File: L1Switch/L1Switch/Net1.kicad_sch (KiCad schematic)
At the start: 31 parts, among them J2 Conn_01x07_Male, U2 VSC8658

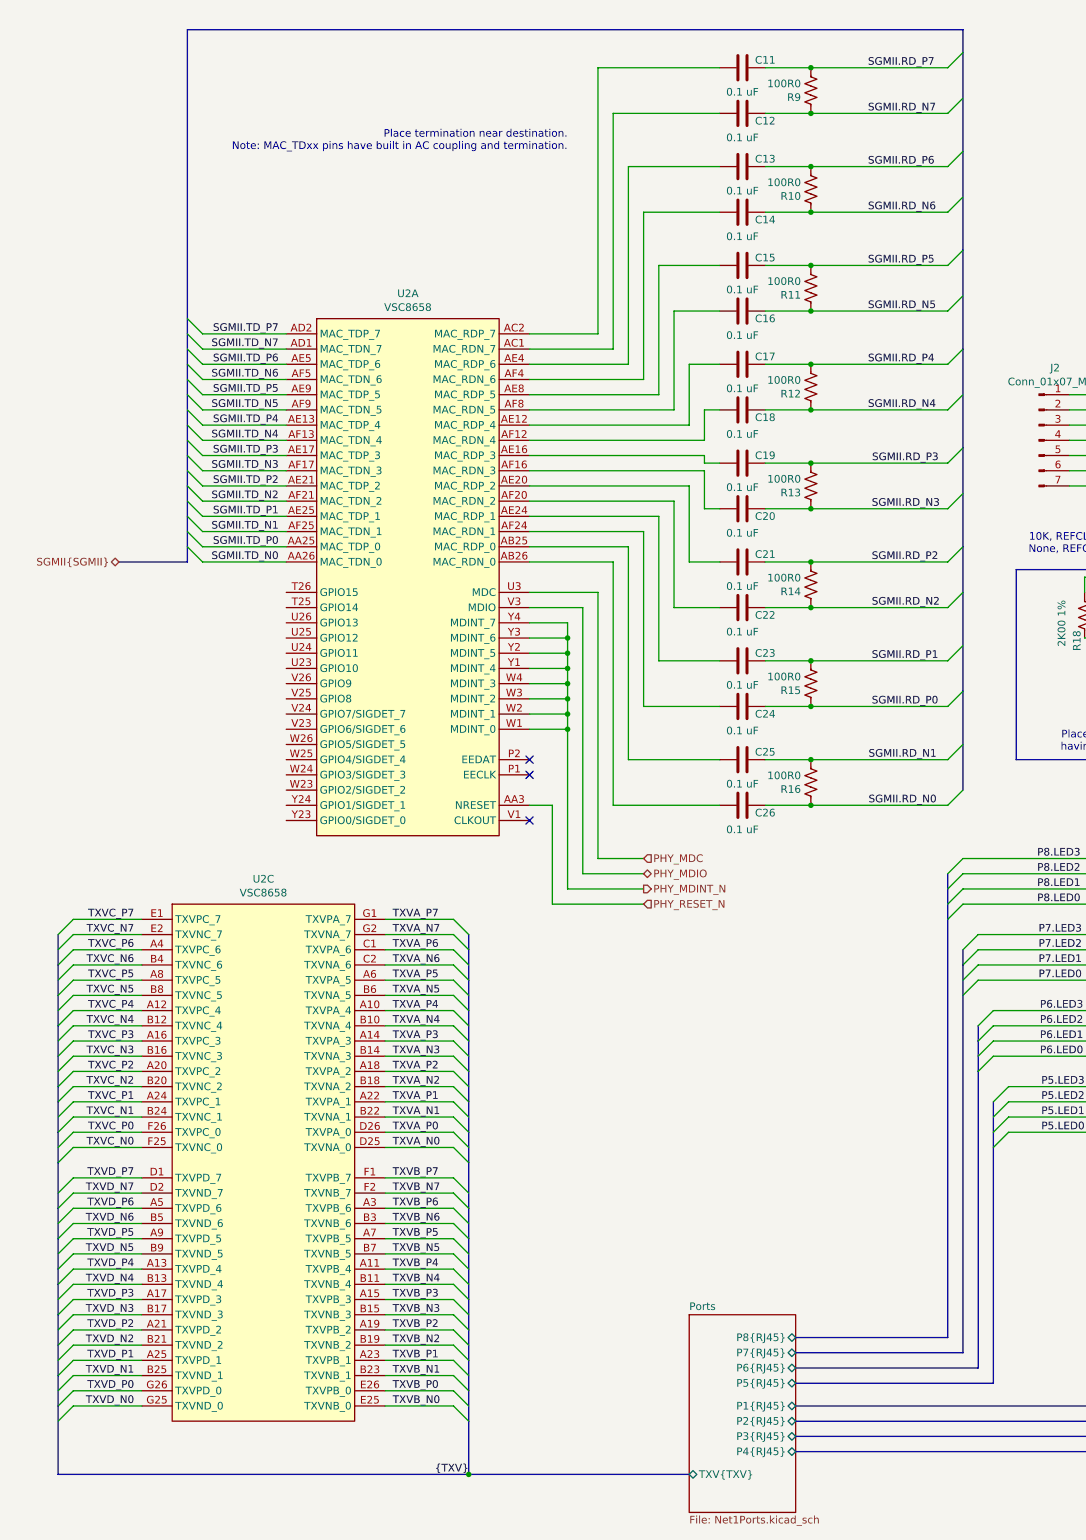
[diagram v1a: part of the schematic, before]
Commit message: SGMII 0 Rx/Tx routed to FPGA.
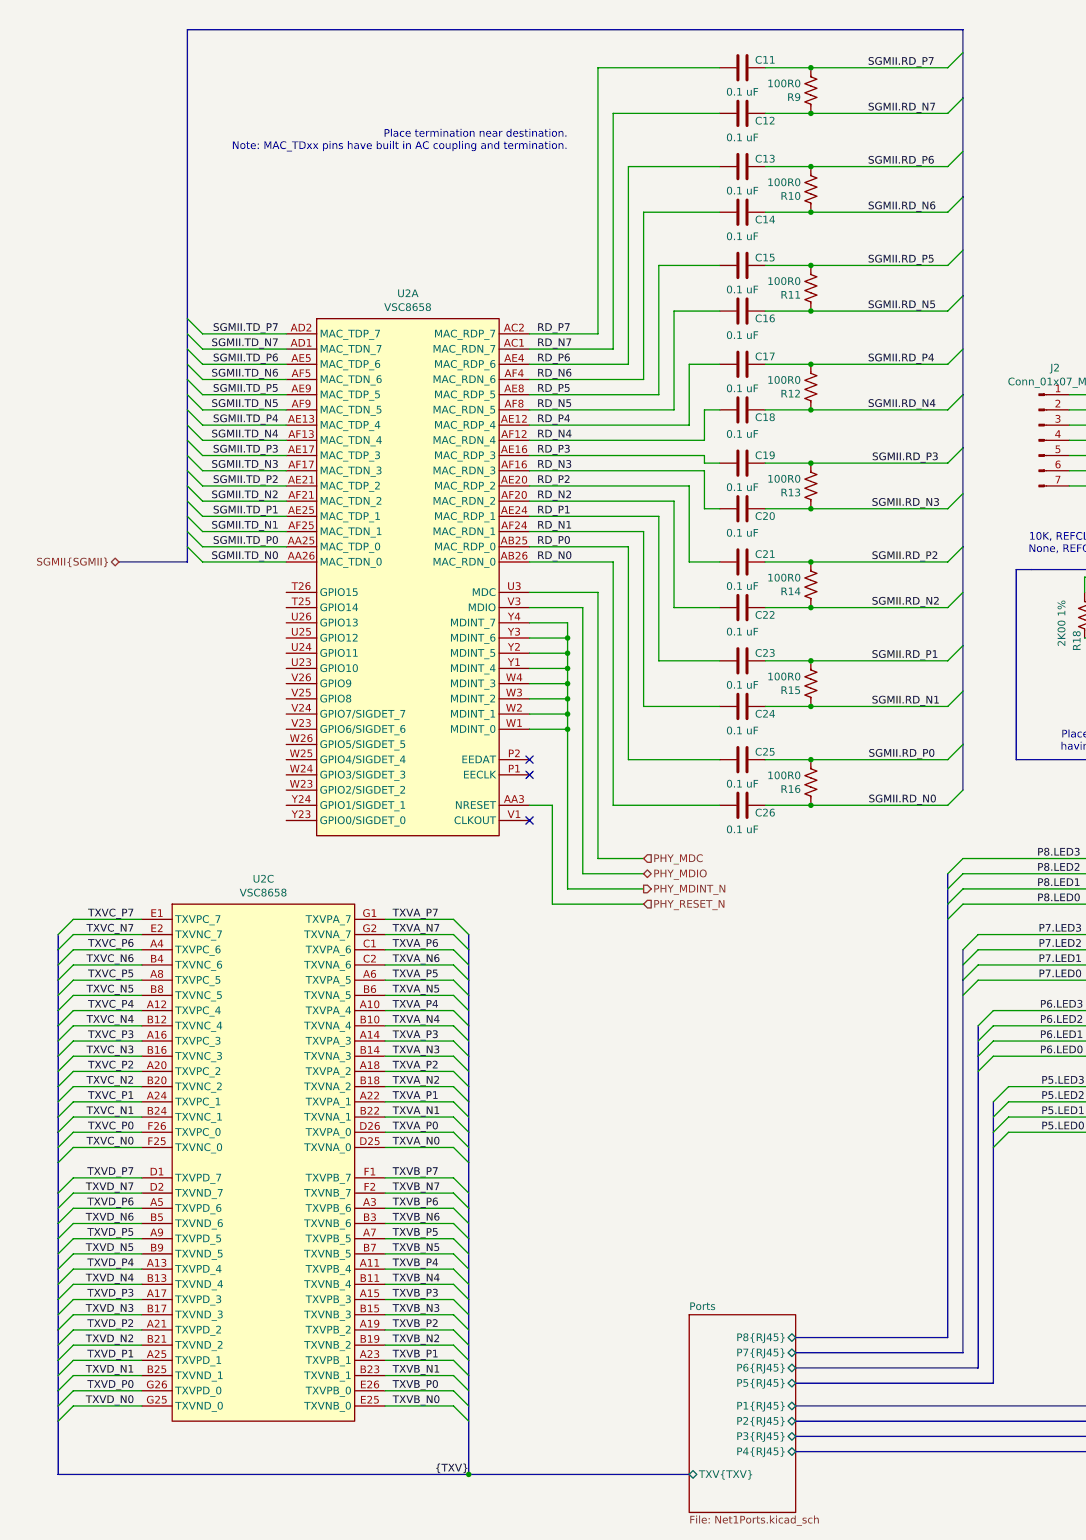
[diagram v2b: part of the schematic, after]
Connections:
- net SGMII.RD_N1: now also C24.1, R15.1; no longer C25.1, R16.2
- net SGMII.RD_P0: now also C25.1, R16.2; no longer C24.1, R15.1
- net RD_P0: now reaches C25.2, U2.AB25 (MAC_RDP_0)
- net RD_N0: now reaches C26.2, U2.AB26 (MAC_RDN_0)
- net RD_N7: now reaches C12.2, U2.AC1 (MAC_RDN_7)
- net RD_P7: now reaches C11.2, U2.AC2 (MAC_RDP_7)
- net RD_P4: now reaches C17.2, U2.AE12 (MAC_RDP_4)
- net RD_P3: now reaches C19.2, U2.AE16 (MAC_RDP_3)
- net RD_P2: now reaches C21.2, U2.AE20 (MAC_RDP_2)
- net RD_P1: now reaches C23.2, U2.AE24 (MAC_RDP_1)
- net RD_P6: now reaches C13.2, U2.AE4 (MAC_RDP_6)
- net RD_P5: now reaches C15.2, U2.AE8 (MAC_RDP_5)
- net RD_N4: now reaches C18.2, U2.AF12 (MAC_RDN_4)
- net RD_N3: now reaches C20.2, U2.AF16 (MAC_RDN_3)
- net RD_N2: now reaches C22.2, U2.AF20 (MAC_RDN_2)
- net RD_N1: now reaches C24.2, U2.AF24 (MAC_RDN_1)
- net RD_N6: now reaches C14.2, U2.AF4 (MAC_RDN_6)
- net RD_N5: now reaches C16.2, U2.AF8 (MAC_RDN_5)

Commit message: Add decoupling caps and ferrite bead. Clean up reference designators.
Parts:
- added C100, C101, C102, C103, C104, C105, C106, C107, C108, C109, C110, C111, C112, C113, C114, C115, C116, C117, C118, C119, C120, C94, C95, C96, C97, C98, C99: 100nF, Capacitor_SMD:C_0402_1005Metric, symbol Device:C
- added FB1: 100 ohm @ 100 MHz, 3A, L1Switch:FB_1206_3216Metric, symbol Device:Ferrite_Bead
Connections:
- net +1V2: now also C102.1, C103.1, C104.1, C105.1, C106.1, C107.1, C108.1, C109.1, C120.1, FB1.2
- net +1V2A: now also C100.1, C101.1, C118.1, C119.1, C94.1, C95.1, C96.1, C97.1, C98.1, C99.1, FB1.1
- net +3V3: now also C110.1, C111.1, C112.1, C113.1, C114.1, C115.1, C116.1, C117.1
- net GND: now also U2.H25 (CMODE7), U2.J24 (CMODE6), U2.J25 (CMODE5), U2.J26 (CMODE4), U2.K24 (CMODE3), U2.K25 (CMODE2), U2.K26 (CMODE1), U2.L24 (CMODE0), C100.2, C101.2, C102.2, C103.2, C104.2, C105.2, C106.2, C107.2, C108.2, C109.2, C110.2, C111.2, C112.2, C113.2, C114.2, C115.2, C116.2, C117.2, C118.2, C119.2, C120.2, C94.2, C95.2, C96.2, C97.2, C98.2, C99.2
- no-connect marks 37 -> 53
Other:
- note added: "Local decoupling. Place under chip on bottom side."
- moved on the sheet: U2D, U2E, U2H

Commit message: Layout replicated to Net2.
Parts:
- renumbered C11 to C121, C12 to C122, C13 to C123, C14 to C124, C15 to C125, C16 to C126, C17 to C127, C18 to C128, C19 to C129, C20 to C130, C21 to C131, C22 to C132, C23 to C133, C24 to C134, C25 to C135, C26 to C136, C27 to C137, C28 to C138, C94 to C139, C95 to C140, C96 to C141, C97 to C142, C98 to C143, C99 to C144, C100 to C145, C101 to C146, C118 to C147, C119 to C148, C120 to C149, C102 to C150, C103 to C151, C104 to C152, C105 to C153, C106 to C154, C107 to C155, C108 to C156, C109 to C157, C110 to C158, C111 to C159, C112 to C160, C113 to C161, C114 to C162, C115 to C163, C116 to C164, C117 to C165, FB1 to FB2, J2 to J4, R9 to R76, R10 to R77, R11 to R78, R12 to R79, R13 to R80, R14 to R81, R15 to R82, R16 to R83, R18 to R84, R19 to R85, R20 to R86, U2 to U7
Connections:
- net +1V2: now also U7.AB25 (MAC_RDP_0), U7.AB26 (MAC_RDN_0), U7.AC1 (MAC_RDN_7), U7.AC2 (MAC_RDP_7), U7.AE12 (MAC_RDP_4), U7.AE16 (MAC_RDP_3), U7.AE20 (MAC_RDP_2), U7.AE24 (MAC_RDP_1), U7.AE4 (MAC_RDP_6), U7.AE8 (MAC_RDP_5), U7.AF12 (MAC_RDN_4), U7.AF16 (MAC_RDN_3), U7.AF20 (MAC_RDN_2), U7.AF24 (MAC_RDN_1), U7.AF4 (MAC_RDN_6), U7.AF8 (MAC_RDN_5), U7.U3 (MDC), U7.V3 (MDIO), U7.W2 (MDINT_1), U7.W3 (MDINT_2), U7.W4 (MDINT_3), U7.Y1 (MDINT_4), U7.Y2 (MDINT_5), U7.Y3 (MDINT_6), U7.Y4 (MDINT_7); no longer U7.K19 (VDD12), U7.K8 (VDD12), U7.L19 (VDD12), U7.L8 (VDD12), U7.M19 (VDD12), U7.M8 (VDD12), U7.N19 (VDD12), U7.N8 (VDD12), U7.P19 (VDD12), U7.P8 (VDD12), U7.R19 (VDD12), U7.R8 (VDD12), U7.T19 (VDD12), U7.T8 (VDD12), U7.U10 (VDD12), U7.U11 (VDD12), U7.U12 (VDD12), U7.U13 (VDD12), U7.U14 (VDD12), U7.U15 (VDD12), U7.U16 (VDD12), U7.U17 (VDD12), U7.U18 (VDD12), U7.U19 (VDD12), U7.U8 (VDD12), U7.U9 (VDD12)
- net +1V2A: now also U7.AA25 (MAC_TDP_0), U7.AA26 (MAC_TDN_0), U7.AD1 (MAC_TDN_7), U7.AD2 (MAC_TDP_7), U7.AE13 (MAC_TDP_4), U7.AE17 (MAC_TDP_3), U7.AE21 (MAC_TDP_2), U7.AE25 (MAC_TDP_1), U7.AE5 (MAC_TDP_6), U7.AE9 (MAC_TDP_5), U7.AF13 (MAC_TDN_4), U7.AF17 (MAC_TDN_3), U7.AF21 (MAC_TDN_2), U7.AF25 (MAC_TDN_1), U7.AF5 (MAC_TDN_6), U7.AF9 (MAC_TDN_5), U7.T25 (GPIO14), U7.T26 (GPIO15), U7.U23 (GPIO10), U7.U24 (GPIO11), U7.U25 (GPIO12), U7.U26 (GPIO13), U7.V23 (GPIO6/SIGDET_6), U7.V24 (GPIO7/SIGDET_7), U7.V25 (GPIO8), U7.V26 (GPIO9), U7.W25 (GPIO4/SIGDET_4), U7.W26 (GPIO5/SIGDET_5); no longer U7.AB24 (VDD12A), U7.AC11 (VDD12A), U7.AC12 (VDD12A), U7.AC13 (VDD12A), U7.AC15 (VDD12A), U7.AC16 (VDD12A), U7.AC18 (VDD12A), U7.AC19 (VDD12A), U7.AC20 (VDD12A), U7.AC24 (VDD12A), U7.AC4 (VDD12A), U7.AC5 (VDD12A), U7.AC7 (VDD12A), U7.AC8 (VDD12A), U7.AD19 (VDD12A), U7.AD8 (VDD12A), U7.C13 (VDD12A), U7.C19 (VDD12A), U7.C20 (VDD12A), U7.C7 (VDD12A), U7.D13 (VDD12A), U7.D19 (VDD12A), U7.D20 (VDD12A), U7.D23 (VDD12A), U7.D6 (VDD12A), U7.D7 (VDD12A), U7.E24 (VDD12A), U7.E3 (VDD12A), U7.E4 (VDD12A)
- net +3V3: now also U7.AA25 (MAC_TDP_0), U7.AA26 (MAC_TDN_0), U7.AC1 (MAC_RDN_7), U7.AC2 (MAC_RDP_7), U7.AD1 (MAC_TDN_7), U7.AD2 (MAC_TDP_7), U7.AE12 (MAC_RDP_4), U7.AE13 (MAC_TDP_4), U7.AE16 (MAC_RDP_3), U7.AE17 (MAC_TDP_3), U7.AE20 (MAC_RDP_2), U7.AE21 (MAC_TDP_2), U7.AE25 (MAC_TDP_1), U7.AE4 (MAC_RDP_6), U7.AE5 (MAC_TDP_6), U7.AE8 (MAC_RDP_5), U7.AE9 (MAC_TDP_5), U7.AF12 (MAC_RDN_4), U7.AF13 (MAC_TDN_4), U7.AF16 (MAC_RDN_3), U7.AF17 (MAC_TDN_3), U7.AF21 (MAC_TDN_2), U7.AF25 (MAC_TDN_1), U7.AF4 (MAC_RDN_6), U7.AF5 (MAC_TDN_6), U7.AF8 (MAC_RDN_5), U7.AF9 (MAC_TDN_5), U7.P1 (EECLK), U7.P2 (EEDAT), U7.T25 (GPIO14), U7.T26 (GPIO15), U7.U23 (GPIO10), U7.U24 (GPIO11), U7.U25 (GPIO12), U7.U26 (GPIO13), U7.V23 (GPIO6/SIGDET_6), U7.V24 (GPIO7/SIGDET_7), U7.V25 (GPIO8), U7.V26 (GPIO9), U7.W23 (GPIO2/SIGDET_2), U7.W24 (GPIO3/SIGDET_3), U7.W25 (GPIO4/SIGDET_4), U7.W26 (GPIO5/SIGDET_5), U7.Y23 (GPIO0/SIGDET_0), U7.Y24 (GPIO1/SIGDET_1); no longer U7.AA23 (VDD33), U7.AB23 (VDD33), U7.AB4 (VDDIO), U7.AD11 (VDD33), U7.AD12 (VDD33), U7.AD14 (VDD33), U7.AD17 (VDD33), U7.AD20 (VDD33), U7.AD21 (VDD33), U7.AD3 (VDD33), U7.AD5 (VDD33), U7.AD7 (VDD33), U7.C10 (VDD33), U7.C11 (VDD33), U7.C12 (VDD33), U7.C16 (VDD33), U7.C17 (VDD33), U7.C21 (VDD33), U7.C23 (VDD33), U7.C25 (VDD33), U7.C3 (VDD33), U7.C4 (VDD33), U7.D10 (VDD33), U7.D11 (VDD33), U7.D12 (VDD33), U7.D16 (VDD33), U7.D17 (VDD33), U7.D21 (VDD33), U7.D22 (VDD33), U7.D3 (VDD33), U7.D4 (VDD33), U7.F24 (VDD33), U7.G23 (VDD33), U7.H23 (VDD33), U7.H24 (VDD33), U7.J23 (VDD33), U7.M23 (VDD33), U7.M24 (VDD33), U7.N1 (VDD33), U7.N2 (VDD33), U7.N3 (VDD33), U7.N4 (VDD33), U7.R25 (VDD33), U7.R26 (VDD33), U7.U2 (VDDIO), U7.U4 (VDD33), U7.V2 (VDDIO)
- net GND: now also U7.AA25 (MAC_TDP_0), U7.AA25 (MAC_TDP_0), U7.AA26 (MAC_TDN_0), U7.AA26 (MAC_TDN_0), U7.AA3 (NRESET), U7.AB25 (MAC_RDP_0), U7.AB25 (MAC_RDP_0), U7.AB26 (MAC_RDN_0), U7.AB26 (MAC_RDN_0), U7.AC1 (MAC_RDN_7), U7.AC1 (MAC_RDN_7), U7.AC2 (MAC_RDP_7), U7.AC2 (MAC_RDP_7), U7.AD1 (MAC_TDN_7), U7.AD1 (MAC_TDN_7), U7.AD2 (MAC_TDP_7), U7.AD2 (MAC_TDP_7), U7.AE12 (MAC_RDP_4), U7.AE12 (MAC_RDP_4), U7.AE13 (MAC_TDP_4), U7.AE13 (MAC_TDP_4), U7.AE16 (MAC_RDP_3), U7.AE16 (MAC_RDP_3), U7.AE17 (MAC_TDP_3), U7.AE17 (MAC_TDP_3), U7.AE20 (MAC_RDP_2), U7.AE20 (MAC_RDP_2), U7.AE21 (MAC_TDP_2), U7.AE21 (MAC_TDP_2), U7.AE24 (MAC_RDP_1), U7.AE24 (MAC_RDP_1), U7.AE25 (MAC_TDP_1), U7.AE25 (MAC_TDP_1), U7.AE4 (MAC_RDP_6), U7.AE4 (MAC_RDP_6), U7.AE5 (MAC_TDP_6), U7.AE5 (MAC_TDP_6), U7.AE8 (MAC_RDP_5), U7.AE8 (MAC_RDP_5), U7.AE9 (MAC_TDP_5), U7.AE9 (MAC_TDP_5), U7.AF12 (MAC_RDN_4), U7.AF12 (MAC_RDN_4), U7.AF13 (MAC_TDN_4), U7.AF13 (MAC_TDN_4), U7.AF16 (MAC_RDN_3), U7.AF16 (MAC_RDN_3), U7.AF17 (MAC_TDN_3), U7.AF17 (MAC_TDN_3), U7.AF20 (MAC_RDN_2), U7.AF20 (MAC_RDN_2), U7.AF21 (MAC_TDN_2), U7.AF21 (MAC_TDN_2), U7.AF24 (MAC_RDN_1), U7.AF24 (MAC_RDN_1), U7.AF25 (MAC_TDN_1), U7.AF25 (MAC_TDN_1), U7.AF4 (MAC_RDN_6), U7.AF4 (MAC_RDN_6), U7.AF5 (MAC_TDN_6), U7.AF5 (MAC_TDN_6), U7.AF8 (MAC_RDN_5), U7.AF8 (MAC_RDN_5), U7.AF9 (MAC_TDN_5), U7.AF9 (MAC_TDN_5), U7.P1 (EECLK), U7.P2 (EEDAT), U7.P2 (EEDAT), U7.T25 (GPIO14), U7.T25 (GPIO14), U7.T26 (GPIO15), U7.T26 (GPIO15), U7.U23 (GPIO10), U7.U23 (GPIO10), U7.U24 (GPIO11), U7.U24 (GPIO11), U7.U25 (GPIO12), U7.U25 (GPIO12), U7.U26 (GPIO13), U7.U26 (GPIO13), U7.U3 (MDC), U7.U3 (MDC), U7.U3 (MDC), U7.V1 (CLKOUT), U7.V23 (GPIO6/SIGDET_6), U7.V23 (GPIO6/SIGDET_6), U7.V24 (GPIO7/SIGDET_7), U7.V24 (GPIO7/SIGDET_7), U7.V25 (GPIO8), U7.V25 (GPIO8), U7.V26 (GPIO9), U7.V26 (GPIO9), U7.V3 (MDIO), U7.V3 (MDIO), U7.V3 (MDIO), U7.W1 (MDINT_0), U7.W1 (MDINT_0), U7.W2 (MDINT_1), U7.W2 (MDINT_1), U7.W23 (GPIO2/SIGDET_2), U7.W23 (GPIO2/SIGDET_2), U7.W24 (GPIO3/SIGDET_3), U7.W24 (GPIO3/SIGDET_3), U7.W25 (GPIO4/SIGDET_4), U7.W25 (GPIO4/SIGDET_4), U7.W26 (GPIO5/SIGDET_5), U7.W26 (GPIO5/SIGDET_5), U7.W3 (MDINT_2), U7.W3 (MDINT_2), U7.W3 (MDINT_2), U7.W4 (MDINT_3), U7.W4 (MDINT_3), U7.W4 (MDINT_3), U7.Y1 (MDINT_4), U7.Y1 (MDINT_4), U7.Y1 (MDINT_4), U7.Y2 (MDINT_5), U7.Y2 (MDINT_5), U7.Y2 (MDINT_5), U7.Y23 (GPIO0/SIGDET_0), U7.Y24 (GPIO1/SIGDET_1), U7.Y24 (GPIO1/SIGDET_1), U7.Y3 (MDINT_6), U7.Y3 (MDINT_6), U7.Y3 (MDINT_6), U7.Y4 (MDINT_7), U7.Y4 (MDINT_7), U7.Y4 (MDINT_7); no longer U7.A2 (VSS), U7.AA24 (VSS), U7.AA4 (VSS), U7.AB3 (VSS), U7.AC10 (VSS), U7.AC14 (VSS), U7.AC17 (VSS), U7.AC21 (VSS), U7.AC22 (VSS), U7.AC23 (VSS), U7.AC3 (VSS), U7.AC6 (VSS), U7.AC9 (VSS), U7.AD10 (VSS), U7.AD13 (VSS), U7.AD15 (VSS), U7.AD16 (VSS), U7.AD18 (VSS), U7.AD22 (VSS), U7.AD23 (VSS), U7.AD24 (VSS), U7.AD4 (VSS), U7.AD6 (VSS), U7.AD9 (VSS), U7.AE1 (VSS), U7.AE26 (VSS), U7.B1 (VSS), U7.B2 (VSS), U7.B26 (VSS), U7.C14 (VSS), U7.C15 (VSS), U7.C18 (VSS), U7.C24 (VSS), U7.C26 (VSS), U7.C5 (VSS), U7.C8 (VSS), U7.C9 (VSS), U7.D14 (VSS), U7.D15 (VSS), U7.D18 (VSS), U7.D24 (VSS), U7.D5 (VSS), U7.D8 (VSS), U7.D9 (VSS), U7.F3 (VSS), U7.H1 (VSS), U7.H2 (VSS), U7.H25 (CMODE7), U7.H26 (VSS), U7.H3 (VSS), U7.H4 (VSS), U7.J24 (CMODE6), U7.J25 (CMODE5), U7.J26 (CMODE4), U7.K1 (VSS), U7.K10 (VSS), U7.K11 (VSS), U7.K12 (VSS), U7.K13 (VSS), U7.K14 (VSS), U7.K15 (VSS), U7.K16 (VSS), U7.K17 (VSS), U7.K18 (VSS), U7.K2 (VSS), U7.K23 (VSS), U7.K24 (CMODE3), U7.K25 (CMODE2), U7.K26 (CMODE1), U7.K9 (VSS), U7.L10 (VSS), U7.L11 (VSS), U7.L12 (VSS), U7.L13 (VSS), U7.L14 (VSS), U7.L15 (VSS), U7.L16 (VSS), U7.L17 (VSS), U7.L18 (VSS), U7.L23 (VSS), U7.L24 (CMODE0), U7.L9 (VSS), U7.M10 (VSS), U7.M11 (VSS), U7.M12 (VSS), U7.M13 (VSS), U7.M14 (VSS), U7.M15 (VSS), U7.M16 (VSS), U7.M17 (VSS), U7.M18 (VSS), U7.M9 (VSS), U7.N10 (VSS), U7.N11 (VSS), U7.N12 (VSS), U7.N13 (VSS), U7.N14 (VSS), U7.N15 (VSS), U7.N16 (VSS), U7.N17 (VSS), U7.N18 (VSS), U7.N9 (VSS), U7.P10 (VSS), U7.P11 (VSS), U7.P12 (VSS), U7.P13 (VSS), U7.P14 (VSS), U7.P15 (VSS), U7.P16 (VSS), U7.P17 (VSS), U7.P18 (VSS), U7.P9 (VSS), U7.R10 (VSS), U7.R11 (VSS), U7.R12 (VSS), U7.R13 (VSS), U7.R14 (VSS), U7.R15 (VSS), U7.R16 (VSS), U7.R17 (VSS), U7.R18 (VSS), U7.R9 (VSS), U7.T10 (VSS), U7.T11 (VSS), U7.T12 (VSS), U7.T13 (VSS), U7.T14 (VSS), U7.T15 (VSS), U7.T16 (VSS), U7.T17 (VSS), U7.T18 (VSS), U7.T9 (VSS), U7.V4 (VSS), U7.Y25 (VSS), U7.Y26 (VSS)
- net P1.LED0: now also U7.V3 (MDIO); no longer U7.L26 (LED_0_0)
- net P1.LED1: now also U7.U3 (MDC); no longer U7.L25 (LED_0_1)
- net P1.LED2: no longer U7.M26 (LED_0_2)
- net P1.LED3: now also U7.AB26 (MAC_RDN_0); no longer U7.M25 (LED_0_3)
- net P2.LED0: now also U7.AF24 (MAC_RDN_1); no longer U7.N26 (LED_1_0)
- net P2.LED1: now also U7.AE24 (MAC_RDP_1); no longer U7.N25 (LED_1_1)
- net P2.LED2: now also U7.AF20 (MAC_RDN_2); no longer U7.P26 (LED_1_2)
- net P2.LED3: now also U7.AE20 (MAC_RDP_2); no longer U7.P25 (LED_1_3)
- net P3.LED0: now also U7.AE16 (MAC_RDP_3); no longer U7.N24 (LED_2_0)
- net P3.LED1: now also U7.AF12 (MAC_RDN_4); no longer U7.N23 (LED_2_1)
- net P3.LED2: now also U7.AE12 (MAC_RDP_4); no longer U7.P24 (LED_2_2)
- net P3.LED3: now also U7.AF8 (MAC_RDN_5); no longer U7.P23 (LED_2_3)
- net P4.LED0: now also U7.AF4 (MAC_RDN_6); no longer U7.R24 (LED_3_0)
- net P4.LED1: now also U7.AE4 (MAC_RDP_6); no longer U7.R23 (LED_3_1)
- net P4.LED2: now also U7.AC1 (MAC_RDN_7); no longer U7.T24 (LED_3_2)
- net P4.LED3: now also U7.AC2 (MAC_RDP_7); no longer U7.T23 (LED_3_3)
- net P5.LED0: now also U7.T25 (GPIO14); no longer U7.R4 (LED_4_0)
- net P5.LED1: now also U7.T26 (GPIO15); no longer U7.R3 (LED_4_1)
- net P5.LED2: no longer U7.P4 (LED_4_2)
- net P5.LED3: now also U7.AA26 (MAC_TDN_0); no longer U7.P3 (LED_4_3)
- net P6.LED0: now also U7.AF25 (MAC_TDN_1); no longer U7.M4 (LED_5_0)
- net P6.LED1: now also U7.AE25 (MAC_TDP_1); no longer U7.M3 (LED_5_1)
- net P6.LED2: now also U7.AF21 (MAC_TDN_2); no longer U7.L4 (LED_5_2)
- net P6.LED3: now also U7.AE21 (MAC_TDP_2); no longer U7.L3 (LED_5_3)
- net P7.LED0: now also U7.AE17 (MAC_TDP_3); no longer U7.M2 (LED_6_0)
- net P7.LED1: now also U7.AF13 (MAC_TDN_4); no longer U7.M1 (LED_6_1)
- net P7.LED2: now also U7.AE13 (MAC_TDP_4); no longer U7.L2 (LED_6_2)
- net P7.LED3: now also U7.AF9 (MAC_TDN_5); no longer U7.L1 (LED_6_3)
- net P8.LED0: now also U7.AF5 (MAC_TDN_6); no longer U7.K4 (LED_7_0)
- net P8.LED1: now also U7.AE5 (MAC_TDP_6); no longer U7.K3 (LED_7_1)
- net P8.LED2: now also U7.AD1 (MAC_TDN_7); no longer U7.J4 (LED_7_2)
- net P8.LED3: now also U7.AD2 (MAC_TDP_7); no longer U7.J3 (LED_7_3)
- net PHY_REFCLK: now also U7.V26 (GPIO9); no longer U7.J1 (XTAL1/REFCLK)
- net TXVA_N0: now also U7.AB26 (MAC_RDN_0); no longer U7.D25 (TXVNA_0)
- net TXVA_N1: now also U7.AF24 (MAC_RDN_1); no longer U7.B22 (TXVNA_1)
- net TXVA_N2: now also U7.AF20 (MAC_RDN_2); no longer U7.B18 (TXVNA_2)
- net TXVA_N3: now also U7.AF16 (MAC_RDN_3); no longer U7.B14 (TXVNA_3)
- net TXVA_N4: now also U7.AF12 (MAC_RDN_4); no longer U7.B10 (TXVNA_4)
- net TXVA_N5: now also U7.AF8 (MAC_RDN_5); no longer U7.B6 (TXVNA_5)
- net TXVA_N6: now also U7.AF4 (MAC_RDN_6); no longer U7.C2 (TXVNA_6)
- net TXVA_N7: now also U7.AC1 (MAC_RDN_7); no longer U7.G2 (TXVNA_7)
- net TXVA_P0: now also U7.AB25 (MAC_RDP_0); no longer U7.D26 (TXVPA_0)
- net TXVA_P1: now also U7.AE24 (MAC_RDP_1); no longer U7.A22 (TXVPA_1)
- net TXVA_P2: now also U7.AE20 (MAC_RDP_2); no longer U7.A18 (TXVPA_2)
- net TXVA_P3: now also U7.AE16 (MAC_RDP_3); no longer U7.A14 (TXVPA_3)
- net TXVA_P4: now also U7.AE12 (MAC_RDP_4); no longer U7.A10 (TXVPA_4)
- net TXVA_P5: now also U7.AE8 (MAC_RDP_5); no longer U7.A6 (TXVPA_5)
- net TXVA_P6: now also U7.AE4 (MAC_RDP_6); no longer U7.C1 (TXVPA_6)
- net TXVA_P7: now also U7.AC2 (MAC_RDP_7); no longer U7.G1 (TXVPA_7)
- net TXVB_N0: now also U7.V1 (CLKOUT); no longer U7.E25 (TXVNB_0)
- net TXVB_N1: no longer U7.B23 (TXVNB_1)
- net TXVB_N2: now also U7.P2 (EEDAT); no longer U7.B19 (TXVNB_2)
- net TXVB_N3: now also U7.W1 (MDINT_0); no longer U7.B15 (TXVNB_3)
- net TXVB_N4: now also U7.W3 (MDINT_2); no longer U7.B11 (TXVNB_4)
- net TXVB_N5: now also U7.Y1 (MDINT_4); no longer U7.B7 (TXVNB_5)
- net TXVB_N6: now also U7.Y3 (MDINT_6); no longer U7.B3 (TXVNB_6)
- net TXVB_N7: now also U7.V3 (MDIO); no longer U7.F2 (TXVNB_7)
- net TXVB_P0: now also U7.AA3 (NRESET); no longer U7.E26 (TXVPB_0)
- net TXVB_P1: now also U7.P1 (EECLK); no longer U7.A23 (TXVPB_1)
- net TXVB_P2: no longer U7.A19 (TXVPB_2)
- net TXVB_P3: now also U7.W2 (MDINT_1); no longer U7.A15 (TXVPB_3)
- net TXVB_P4: now also U7.W4 (MDINT_3); no longer U7.A11 (TXVPB_4)
- net TXVB_P5: now also U7.Y2 (MDINT_5); no longer U7.A7 (TXVPB_5)
- net TXVB_P6: now also U7.Y4 (MDINT_7); no longer U7.A3 (TXVPB_6)
- net TXVB_P7: now also U7.U3 (MDC); no longer U7.F1 (TXVPB_7)
- net TXVC_N0: now also U7.AA26 (MAC_TDN_0); no longer U7.F25 (TXVNC_0)
- net TXVC_N1: now also U7.AF25 (MAC_TDN_1); no longer U7.B24 (TXVNC_1)
- net TXVC_N2: now also U7.AF21 (MAC_TDN_2); no longer U7.B20 (TXVNC_2)
- net TXVC_N3: now also U7.AF17 (MAC_TDN_3); no longer U7.B16 (TXVNC_3)
- net TXVC_N4: now also U7.AF13 (MAC_TDN_4); no longer U7.B12 (TXVNC_4)
- net TXVC_N5: now also U7.AF9 (MAC_TDN_5); no longer U7.B8 (TXVNC_5)
- net TXVC_N6: now also U7.AF5 (MAC_TDN_6); no longer U7.B4 (TXVNC_6)
- net TXVC_N7: now also U7.AD1 (MAC_TDN_7); no longer U7.E2 (TXVNC_7)
- net TXVC_P0: now also U7.AA25 (MAC_TDP_0); no longer U7.F26 (TXVPC_0)
- net TXVC_P1: now also U7.AE25 (MAC_TDP_1); no longer U7.A24 (TXVPC_1)
- net TXVC_P2: now also U7.AE21 (MAC_TDP_2); no longer U7.A20 (TXVPC_2)
- net TXVC_P3: now also U7.AE17 (MAC_TDP_3); no longer U7.A16 (TXVPC_3)
- net TXVC_P4: now also U7.AE13 (MAC_TDP_4); no longer U7.A12 (TXVPC_4)
- net TXVC_P5: now also U7.AE9 (MAC_TDP_5); no longer U7.A8 (TXVPC_5)
- net TXVC_P6: now also U7.AE5 (MAC_TDP_6); no longer U7.A4 (TXVPC_6)
- net TXVC_P7: now also U7.AD2 (MAC_TDP_7); no longer U7.E1 (TXVPC_7)
- net TXVD_N0: now also U7.Y23 (GPIO0/SIGDET_0); no longer U7.G25 (TXVND_0)
- net TXVD_N1: now also U7.W23 (GPIO2/SIGDET_2); no longer U7.B25 (TXVND_1)
- net TXVD_N2: now also U7.W25 (GPIO4/SIGDET_4); no longer U7.B21 (TXVND_2)
- net TXVD_N3: now also U7.V23 (GPIO6/SIGDET_6); no longer U7.B17 (TXVND_3)
- net TXVD_N4: now also U7.V25 (GPIO8); no longer U7.B13 (TXVND_4)
- net TXVD_N5: now also U7.U23 (GPIO10); no longer U7.B9 (TXVND_5)
- net TXVD_N6: now also U7.U25 (GPIO12); no longer U7.B5 (TXVND_6)
- net TXVD_N7: now also U7.T25 (GPIO14); no longer U7.D2 (TXVND_7)
- net TXVD_P0: now also U7.Y24 (GPIO1/SIGDET_1); no longer U7.G26 (TXVPD_0)
- net TXVD_P1: now also U7.W24 (GPIO3/SIGDET_3); no longer U7.A25 (TXVPD_1)
- net TXVD_P2: now also U7.W26 (GPIO5/SIGDET_5); no longer U7.A21 (TXVPD_2)
- net TXVD_P3: now also U7.V24 (GPIO7/SIGDET_7); no longer U7.A17 (TXVPD_3)
- net TXVD_P4: now also U7.V26 (GPIO9); no longer U7.A13 (TXVPD_4)
- net TXVD_P5: now also U7.U24 (GPIO11); no longer U7.A9 (TXVPD_5)
- net TXVD_P6: now also U7.U26 (GPIO13); no longer U7.A5 (TXVPD_6)
- net TXVD_P7: now also U7.T26 (GPIO15); no longer U7.D1 (TXVPD_7)
- net at C137.1: now also U7.W24 (GPIO3/SIGDET_3); no longer U7.E23 (REF_FILT_A)
- net at R84.2: now also U7.W25 (GPIO4/SIGDET_4); no longer U7.F23 (REF_REXT_A)
- net at R85.2: now also U7.W23 (GPIO2/SIGDET_2); no longer U7.F4 (REF_REXT_B)
- net at C138.1: now also U7.Y24 (GPIO1/SIGDET_1); no longer U7.G4 (REF_FILT_B)
- net at R86.2: now also U7.V23 (GPIO6/SIGDET_6); no longer U7.R1 (PLLMODE)
- net at J4.4 (Pin_4): now also U7.U26 (GPIO13); no longer U7.T1 (TMS)
- net at J4.5 (Pin_5): now also U7.U25 (GPIO12); no longer U7.T2 (TCK)
- net at J4.6 (Pin_6): now also U7.U24 (GPIO11); no longer U7.T3 (NTRST)
- net at J4.3 (Pin_3): now also U7.T25 (GPIO14); no longer U7.T4 (TDO)
- net at J4.2 (Pin_2): now also U7.T26 (GPIO15); no longer U7.U1 (TDI)

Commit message: Add instance 3 and 4 of the network ports.
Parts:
- renumbered C121 to C206, C122 to C207, C123 to C208, C124 to C209, C125 to C210, C126 to C211, C127 to C212, C128 to C213, C129 to C214, C130 to C215, C131 to C216, C132 to C217, C133 to C218, C134 to C219, C135 to C220, C136 to C221, C137 to C222, C138 to C223, C139 to C224, C140 to C225, C141 to C226, C142 to C227, C143 to C228, C144 to C229, C145 to C230, C146 to C231, C147 to C232, C148 to C233, C149 to C234, C150 to C235, C151 to C236, C152 to C237, C153 to C238, C154 to C239, C155 to C240, C156 to C241, C157 to C242, C158 to C243, C159 to C244, C160 to C245, C161 to C246, C162 to C247, C163 to C248, C164 to C249, C165 to C250, FB2 to FB3, J4 to J6, R76 to R138, R77 to R139, R78 to R140, R79 to R141, R80 to R142, R81 to R143, R82 to R144, R83 to R145, R84 to R146, R85 to R147, R86 to R148, U7 to U8
